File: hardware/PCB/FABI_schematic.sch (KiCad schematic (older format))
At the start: 45 parts, among them J1 AudioJack3_Ground, J10 Conn_01x03_Male, J11 dispaly_connector_91601-304LF, J11_GND1 Conn_01x01_Male, J11_VDD1 Conn_01x01_Male, J11_data1 Conn_01x01_Male, J2 AudioJack3_Ground, J3 AudioJack3_Ground, J4 AudioJack3_Ground, J5 AudioJack3_Ground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

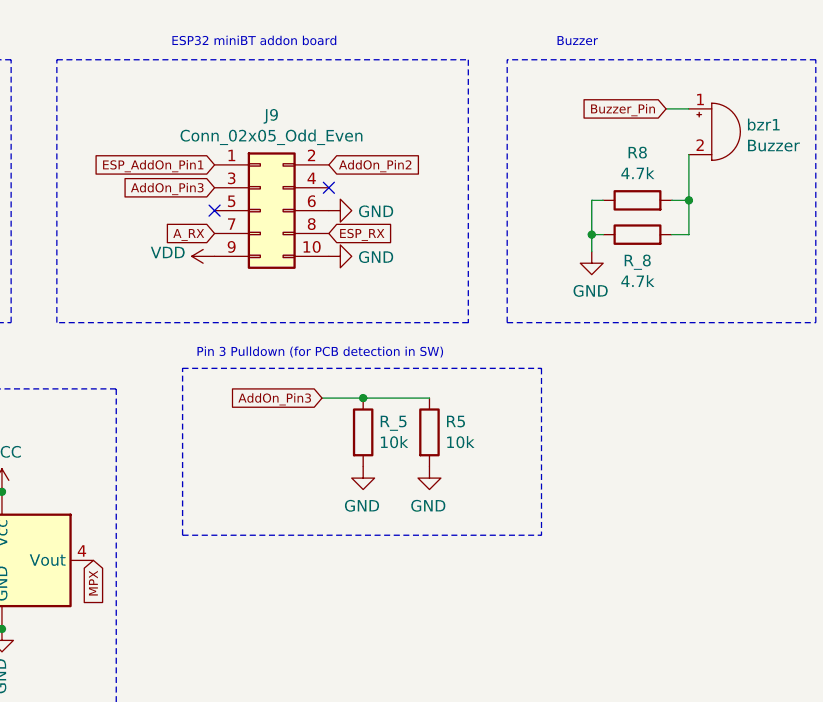
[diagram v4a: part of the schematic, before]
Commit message: PCB: JackPlug footprint adapted: adjuste plastic konb
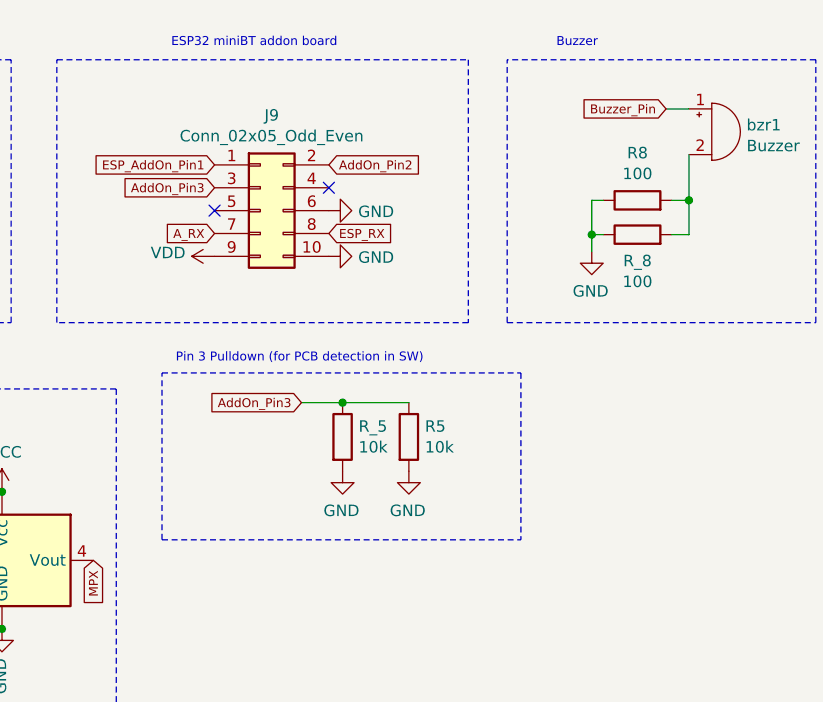
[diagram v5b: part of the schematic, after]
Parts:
- C1: RS-Nr (none) -> 852-3277
- C_1: Farnell-Nr 1327731 -> (none); RS-Nr (none) -> 464-6688
- D1, D2, D3, D4, D5, D6, D7, D8: Farnell (none) -> https://at.farnell.com/littelfuse/p6ke6-8a/tvs-diode/dp/170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; RS-Nr (none) -> 171-9669; RS-components 171-9669 -> (none)
- D11, D12: RS-Nr (none) -> 793-1960
- J1, J2, J3, J4, J5, J6, J7, J8: footprint SamacSys_Parts:FC68125 -> FABI_customLibs:FC68125; RS-Nr (none) -> 805-1655
- J10: RS-Nr (none) -> 251-8092; RS-components 251-8092 -> (none)
- J11: RS-Nr (none) -> 673-7405
- J9: RS-Nr (none) -> 251-8272; RS-components 251-8272 -> (none)
- R1, R3, R5: RS-Nr (none) -> 165-0369
- R2, R4: RS-Nr (none) -> 199-7554
- R6, R7: RS-Nr (none) -> 165-0319
- R8: value 4.7k -> 100; RS-Nr (none) -> 165-0319
- R_1, R_3, R_5: RS-Nr (none) -> 812-3375
- R_2, R_4: RS-Nr (none) -> 905-9694
- R_6, R_7: RS-Nr (none) -> 905-9679
- R_8: value 4.7k -> 100; RS-Nr (none) -> 905-9679
- U1: Farnell-Nr (none) -> 2776055
- bzr1: RS-Nr (none) -> 771-6957; RS-components 771-6957 -> (none)
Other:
- moved on the sheet: R5, R_5

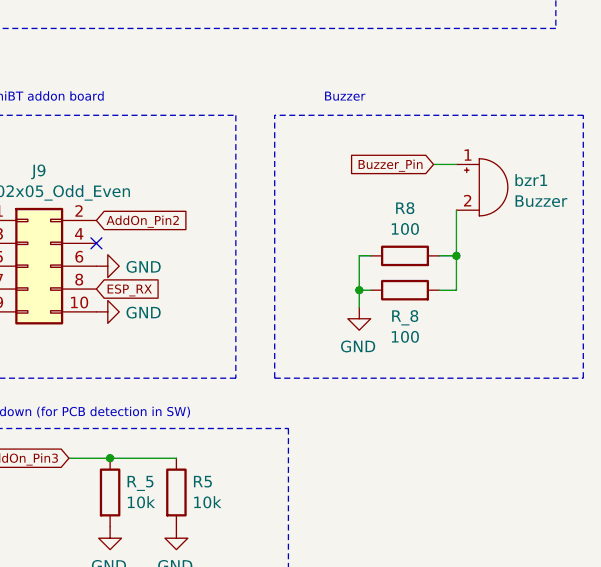
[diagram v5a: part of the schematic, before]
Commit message: PCB update: Footprints and Buzzer Resistior
Signed-off-by: fussthalerandreas <fussthaler.andreas1997@gmail.com>
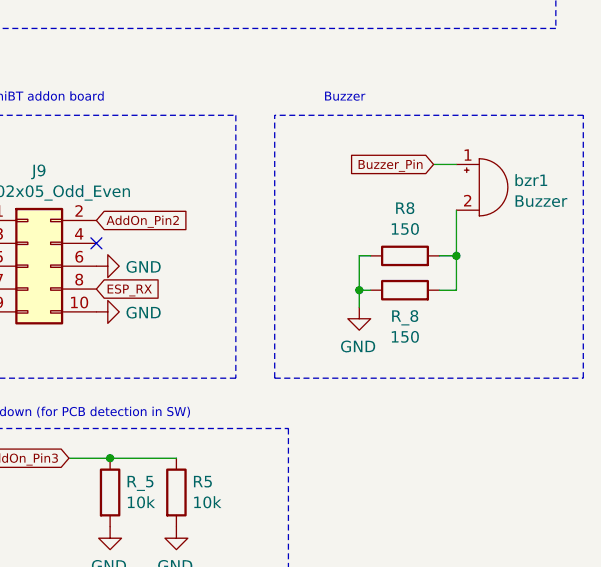
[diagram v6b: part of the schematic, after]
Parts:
- R8, R_8: value 100 -> 150
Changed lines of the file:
@@
 P 9060 4965
 F 0 "R8" V 9267 4965 50  0000 C CNN
-F 1 "100" V 9176 4965 50  0000 C CNN
+F 1 "150" V 9176 4965 50  0000 C CNN
 F 2 "Resistor_THT:R_Axial_DIN0204_L3.6mm_D1.6mm_P7.62mm_Horizontal" V 8990 4965 50  0001 C CNN
 F 3 "~" H 9060 4965 50  0001 C CNN
@@
 P 9060 5115
 F 0 "R_8" V 8945 5115 50  0000 C CNN
-F 1 "100" V 8854 5115 50  0000 C CNN
+F 1 "150" V 8854 5115 50  0000 C CNN
 F 2 "Resistor_SMD:R_0805_2012Metric_Pad1.20x1.40mm_HandSolder" V 8990 5115 50  0001 C CNN
 F 3 "~" H 9060 5115 50  0001 C CNN

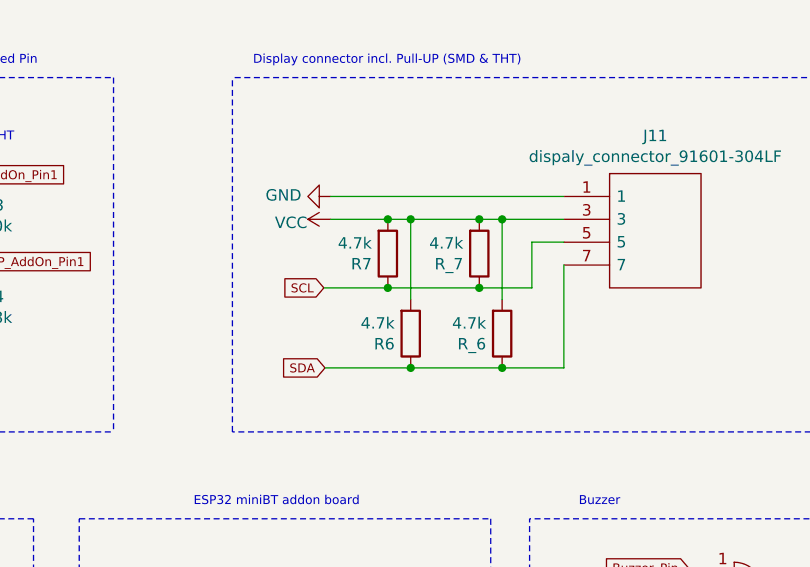
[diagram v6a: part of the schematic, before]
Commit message: 3D casing for PCB version: bottom part created and min changes in top part, PCB and BOM updated (4,7k -> 10k)
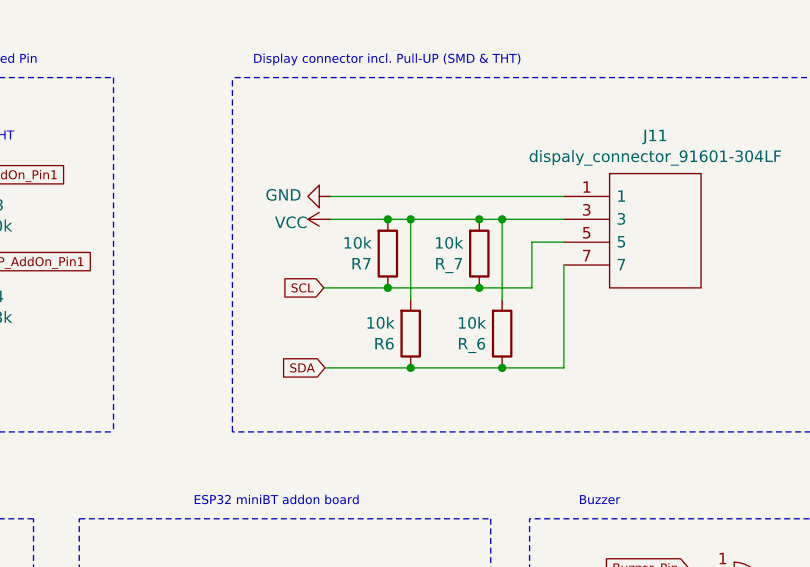
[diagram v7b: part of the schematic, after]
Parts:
- R6, R7, R_6, R_7: value 4.7k -> 10k
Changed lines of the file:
@@
 P 8370 3540
 F 0 "R_6" H 8300 3586 50  0000 R CNN
-F 1 "4.7k" H 8300 3495 50  0000 R CNN
+F 1 "10k" H 8300 3495 50  0000 R CNN
 F 2 "Resistor_SMD:R_0805_2012Metric_Pad1.20x1.40mm_HandSolder" V 8300 3540 50  0001 C CNN
 F 3 "~" H 8370 3540 50  0001 C CNN
@@
 P 8270 3190
 F 0 "R_7" H 8200 3236 50  0000 R CNN
-F 1 "4.7k" H 8200 3145 50  0000 R CNN
+F 1 "10k" H 8200 3145 50  0000 R CNN
 F 2 "Resistor_SMD:R_0805_2012Metric_Pad1.20x1.40mm_HandSolder" V 8200 3190 50  0001 C CNN
 F 3 "~" H 8270 3190 50  0001 C CNN
@@
 P 7870 3190
 F 0 "R7" H 7800 3236 50  0000 R CNN
-F 1 "4.7k" H 7800 3145 50  0000 R CNN
+F 1 "10k" H 7800 3145 50  0000 R CNN
 F 2 "Resistor_THT:R_Axial_DIN0204_L3.6mm_D1.6mm_P7.62mm_Horizontal" V 7800 3190 50  0001 C CNN
 F 3 "~" H 7870 3190 50  0001 C CNN
@@
 P 7970 3540
 F 0 "R6" H 7900 3586 50  0000 R CNN
-F 1 "4.7k" H 7900 3495 50  0000 R CNN
+F 1 "10k" H 7900 3495 50  0000 R CNN
 F 2 "Resistor_THT:R_Axial_DIN0204_L3.6mm_D1.6mm_P7.62mm_Horizontal" V 7900 3540 50  0001 C CNN
 F 3 "~" H 7970 3540 50  0001 C CNN

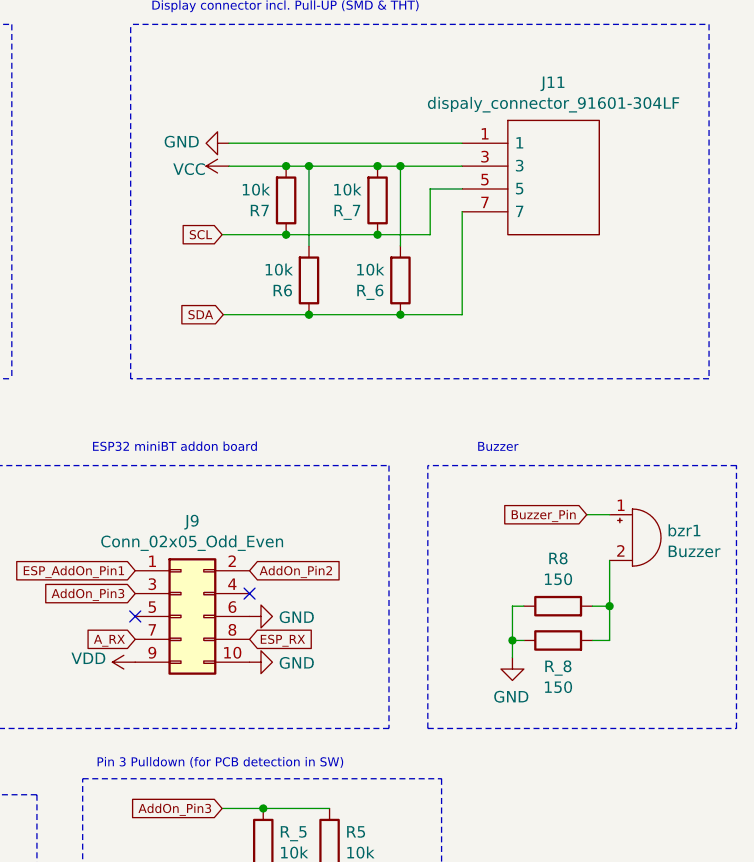
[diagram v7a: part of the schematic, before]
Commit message: PCB: buzzer Resistor & silkscreen updates
Signed-off-by: fussthalerandreas <fussthaler.andreas1997@gmail.com>
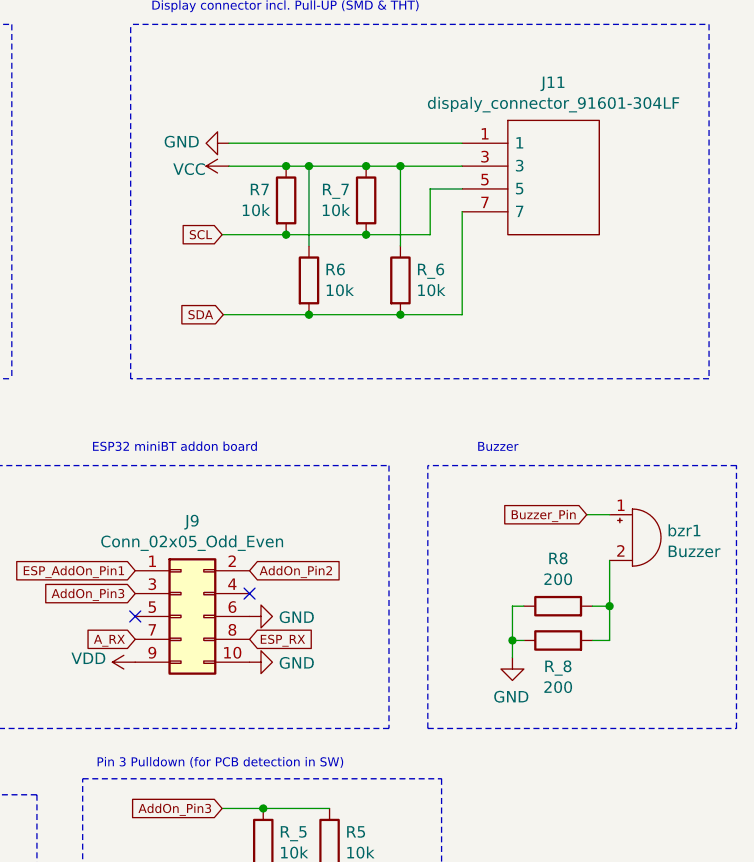
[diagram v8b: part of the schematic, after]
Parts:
- R6, R7: RS https://at.rs-online.com/web/p/widerstande-durchsteckmontage/1650319/ -> https://at.rs-online.com/web/p/widerstande-durchsteckmontage/1650369/; RS-Nr 165-0319 -> 165-0369
- R8: value 150 -> 200; RS https://at.rs-online.com/web/p/widerstande-durchsteckmontage/1650319/ -> https://at.rs-online.com/web/p/widerstande-durchsteckmontage/6833281/; RS-Nr 165-0319 -> 683-3281
- R_6, R_7: RS https://at.rs-online.com/web/p/smd-widerstande/9059679/ -> https://at.rs-online.com/web/p/smd-widerstande/8123375/; RS-Nr 905-9679 -> 812-3375
- R_8: value 150 -> 200; RS https://at.rs-online.com/web/p/smd-widerstande/9059679/ -> https://at.rs-online.com/web/p/smd-widerstande/8101741/; RS-Nr 905-9679 -> 810-1741
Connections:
- net SCL: now also R7.2, R_7.2; no longer R7.1, R_7.1
- net SDA: now also R6.2, R_6.2; no longer R6.1, R_6.1
- net VCC: now also R6.1, R7.1, R_6.1, R_7.1; no longer R6.2, R7.2, R_6.2, R_7.2
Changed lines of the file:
@@
 P 9060 4965
 F 0 "R8" V 9267 4965 50  0000 C CNN
-F 1 "150" V 9176 4965 50  0000 C CNN
+F 1 "200" V 9176 4965 50  0000 C CNN
 F 2 "Resistor_THT:R_Axial_DIN0204_L3.6mm_D1.6mm_P7.62mm_Horizontal" V 8990 4965 50  0001 C CNN
 F 3 "~" H 9060 4965 50  0001 C CNN
-F 4 "https://at.rs-online.com/web/p/widerstande-durchsteckmontage/1650319/" V 9060 4965 50  0001 C CNN "RS"
-F 5 "165-0319" V 9060 4965 50  0001 C CNN "RS-Nr"
+F 4 "https://at.rs-online.com/web/p/widerstande-durchsteckmontage/6833281/" V 9060 4965 50  0001 C CNN "RS"
+F 5 "683-3281" V 9060 4965 50  0001 C CNN "RS-Nr"
 	1    9060 4965
 	0    -1   -1   0
@@
 P 9060 5115
 F 0 "R_8" V 8945 5115 50  0000 C CNN
-F 1 "150" V 8854 5115 50  0000 C CNN
+F 1 "200" V 8854 5115 50  0000 C CNN
 F 2 "Resistor_SMD:R_0805_2012Metric_Pad1.20x1.40mm_HandSolder" V 8990 5115 50  0001 C CNN
 F 3 "~" H 9060 5115 50  0001 C CNN
-F 4 "https://at.rs-online.com/web/p/smd-widerstande/9059679/" V 9060 5115 50  0001 C CNN "RS"
-F 5 "905-9679" V 9060 5115 50  0001 C CNN "RS-Nr"
+F 4 "https://at.rs-online.com/web/p/smd-widerstande/8101741/" V 9060 5115 50  0001 C CNN "RS"
+F 5 "810-1741" V 9060 5115 50  0001 C CNN "RS-Nr"
 	1    9060 5115
 	0    -1   -1   0
@@
 	0    -1   1    0
 $EndComp
-Connection ~ 8270 3040
 Connection ~ 7870 3040
 Wire Wire Line
-	8270 3040 8370 3040
-Wire Wire Line
-	7970 3040 8270 3040
-Wire Wire Line
 	7870 3040 7970 3040
 Wire Wire Line
 	7620 3040 7870 3040
 Wire Wire Line
-	8270 3340 8500 3340
-Wire Wire Line
 	8640 3690 8640 3240
 Wire Wire Line
 	8500 3340 8500 3140
-Connection ~ 8270 3340
-Wire Wire Line
-	7870 3340 8270 3340
 Connection ~ 7870 3340
 Wire Wire Line
@@
 Wire Wire Line
 	7970 3390 7970 3040
-Connection ~ 8370 3690
-Wire Wire Line
-	8370 3690 8640 3690
-$Comp
-L Device:R R_6
-U 1 1 602F9FD4
-P 8370 3540
-F 0 "R_6" H 8300 3586 50  0000 R CNN
-F 1 "10k" H 8300 3495 50  0000 R CNN
-F 2 "Resistor_SMD:R_0805_2012Metric_Pad1.20x1.40mm_HandSolder" V 8300 3540 50  0001 C CNN
-F 3 "~" H 8370 3540 50  0001 C CNN
-F 4 "https://at.rs-online.com/web/p/smd-widerstande/9059679/" H 8370 3540 50  0001 C CNN "RS"
-F 5 "905-9679" H 8370 3540 50  0001 C CNN "RS-Nr"
-	1    8370 3540
-	1    0    0    1
-$EndComp
-Wire Wire Line
-	8370 3690 7970 3690
-$Comp
-L Device:R R_7
-U 1 1 602F7E46
-P 8270 3190
-F 0 "R_7" H 8200 3236 50  0000 R CNN
-F 1 "10k" H 8200 3145 50  0000 R CNN
-F 2 "Resistor_SMD:R_0805_2012Metric_Pad1.20x1.40mm_HandSolder" V 8200 3190 50  0001 C CNN
-F 3 "~" H 8270 3190 50  0001 C CNN
-F 4 "https://at.rs-online.com/web/p/smd-widerstande/9059679/" H 8270 3190 50  0001 C CNN "RS"
-F 5 "905-9679" H 8270 3190 50  0001 C CNN "RS-Nr"
-	1    8270 3190
-	1    0    0    1
-$EndComp
 Wire Wire Line
 	7970 3690 7595 3690
 Connection ~ 7970 3690
-$Comp
-L Device:R R7
-U 1 1 6031DA63
-P 7870 3190
-F 0 "R7" H 7800 3236 50  0000 R CNN
-F 1 "10k" H 7800 3145 50  0000 R CNN
-F 2 "Resistor_THT:R_Axial_DIN0204_L3.6mm_D1.6mm_P7.62mm_Horizontal" V 7800 3190 50  0001 C CNN
-F 3 "~" H 7870 3190 50  0001 C CNN
-F 4 "https://at.rs-online.com/web/p/widerstande-durchsteckmontage/1650319/" H 7870 3190 50  0001 C CNN "RS"
-F 5 "165-0319" H 7870 3190 50  0001 C CNN "RS-Nr"
-	1    7870 3190
-	1    0    0    1
-$EndComp
-$Comp
-L Device:R R6
-U 1 1 6031DA69
-P 7970 3540
-F 0 "R6" H 7900 3586 50  0000 R CNN
-F 1 "10k" H 7900 3495 50  0000 R CNN
-F 2 "Resistor_THT:R_Axial_DIN0204_L3.6mm_D1.6mm_P7.62mm_Horizontal" V 7900 3540 50  0001 C CNN
-F 3 "~" H 7970 3540 50  0001 C CNN
-F 4 "https://at.rs-online.com/web/p/widerstande-durchsteckmontage/1650319/" H 7970 3540 50  0001 C CNN "RS"
-F 5 "165-0319" H 7970 3540 50  0001 C CNN "RS-Nr"
-	1    7970 3540
-	1    0    0    1
-$EndComp
 Text GLabel 5570 5320 0    39   Input ~ 0
 NEOPIXEL
@@
 Text Notes 7040 5680 0    39   ~ 0
 Pin 3 Pulldown (for PCB detection in SW)
+$Comp
+L Device:R R_7
+U 1 1 6074582F
+P 8220 3190
+F 0 "R_7" H 8150 3236 50  0000 R CNN
+F 1 "10k" H 8150 3145 50  0000 R CNN
+F 2 "Resistor_SMD:R_0805_2012Metric_Pad1.20x1.40mm_HandSolder" V 8150 3190 50  0001 C CNN
+F 3 "~" H 8220 3190 50  0001 C CNN
+F 4 "https://at.rs-online.com/web/p/smd-widerstande/8123375/" H 8220 3190 50  0001 C CNN "RS"
+F 5 "812-3375" H 8220 3190 50  0001 C CNN "RS-Nr"
+	1    8220 3190
+	1    0    0    -1
+$EndComp
+Wire Wire Line
+	7870 3340 8220 3340
+Wire Wire Line
+	7970 3040 8220 3040
+Connection ~ 8220 3040
+Wire Wire Line
+	8220 3040 8370 3040
+Connection ~ 8220 3340
+Wire Wire Line
+	8220 3340 8500 3340
+$Comp
+L Device:R R_6
+U 1 1 6074FD21
+P 8370 3540
+F 0 "R_6" H 8440 3586 50  0000 L CNN
+F 1 "10k" H 8440 3495 50  0000 L CNN
+F 2 "Resistor_SMD:R_0805_2012Metric_Pad1.20x1.40mm_HandSolder" V 8300 3540 50  0001 C CNN
+F 3 "~" H 8370 3540 50  0001 C CNN
+F 4 "https://at.rs-online.com/web/p/smd-widerstande/8123375/" H 8370 3540 50  0001 C CNN "RS"
+F 5 "812-3375" H 8370 3540 50  0001 C CNN "RS-Nr"
+	1    8370 3540
+	1    0    0    -1
+$EndComp
+Wire Wire Line
+	7970 3690 8370 3690
+Connection ~ 8370 3690
+Wire Wire Line
+	8370 3690 8640 3690
+$Comp
+L Device:R R7
+U 1 1 6076ABE6
+P 7870 3190
+F 0 "R7" H 7800 3236 50  0000 R CNN
+F 1 "10k" H 7800 3145 50  0000 R CNN
+F 2 "Resistor_THT:R_Axial_DIN0204_L3.6mm_D1.6mm_P7.62mm_Horizontal" V 7800 3190 50  0001 C CNN
+F 3 "~" H 7870 3190 50  0001 C CNN
+F 4 "https://at.rs-online.com/web/p/widerstande-durchsteckmontage/1650369/" H 7870 3190 50  0001 C CNN "RS"
+F 5 "165-0369" H 7870 3190 50  0001 C CNN "RS-Nr"
+	1    7870 3190
+	1    0    0    -1
+$EndComp
+$Comp
+L Device:R R6
+U 1 1 6076FBC9
+P 7970 3540
+F 0 "R6" H 8040 3586 50  0000 L CNN
+F 1 "10k" H 8040 3495 50  0000 L CNN
+F 2 "Resistor_THT:R_Axial_DIN0204_L3.6mm_D1.6mm_P7.62mm_Horizontal" V 7900 3540 50  0001 C CNN
+F 3 "~" H 7970 3540 50  0001 C CNN
+F 4 "https://at.rs-online.com/web/p/widerstande-durchsteckmontage/1650369/" H 7970 3540 50  0001 C CNN "RS"
+F 5 "165-0369" H 7970 3540 50  0001 C CNN "RS-Nr"
+	1    7970 3540
+	1    0    0    -1
+$EndComp
 $EndSCHEMATC
